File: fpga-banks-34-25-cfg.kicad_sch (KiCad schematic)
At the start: 49 parts, among them J13 PinHeader_1x3_P2.54mm_Drill1.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, Q12 2N7002_SOT-23-3, Q13 2N7002_SOT-23-3, Q14 2N7002_SOT-23-3, Q15 2N7002_SOT-23-3, Q16 2N7002_SOT-23-3, U14 XC7A100T-FGG484

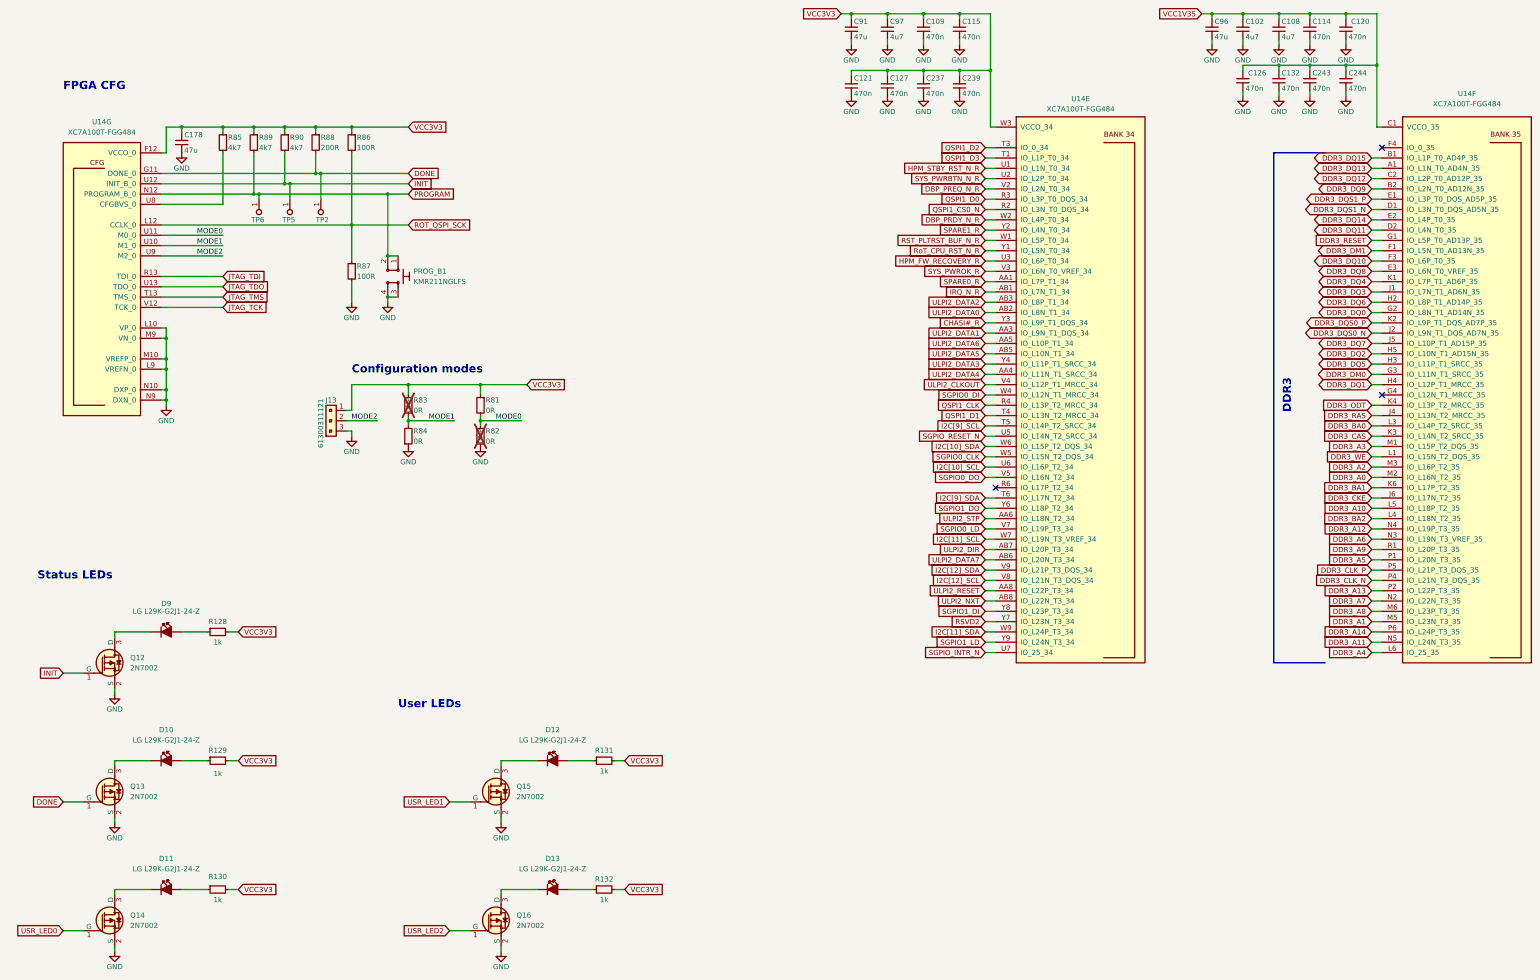
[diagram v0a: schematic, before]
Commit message: [#68236] Update symbols and footprints, clean ERC and DRC
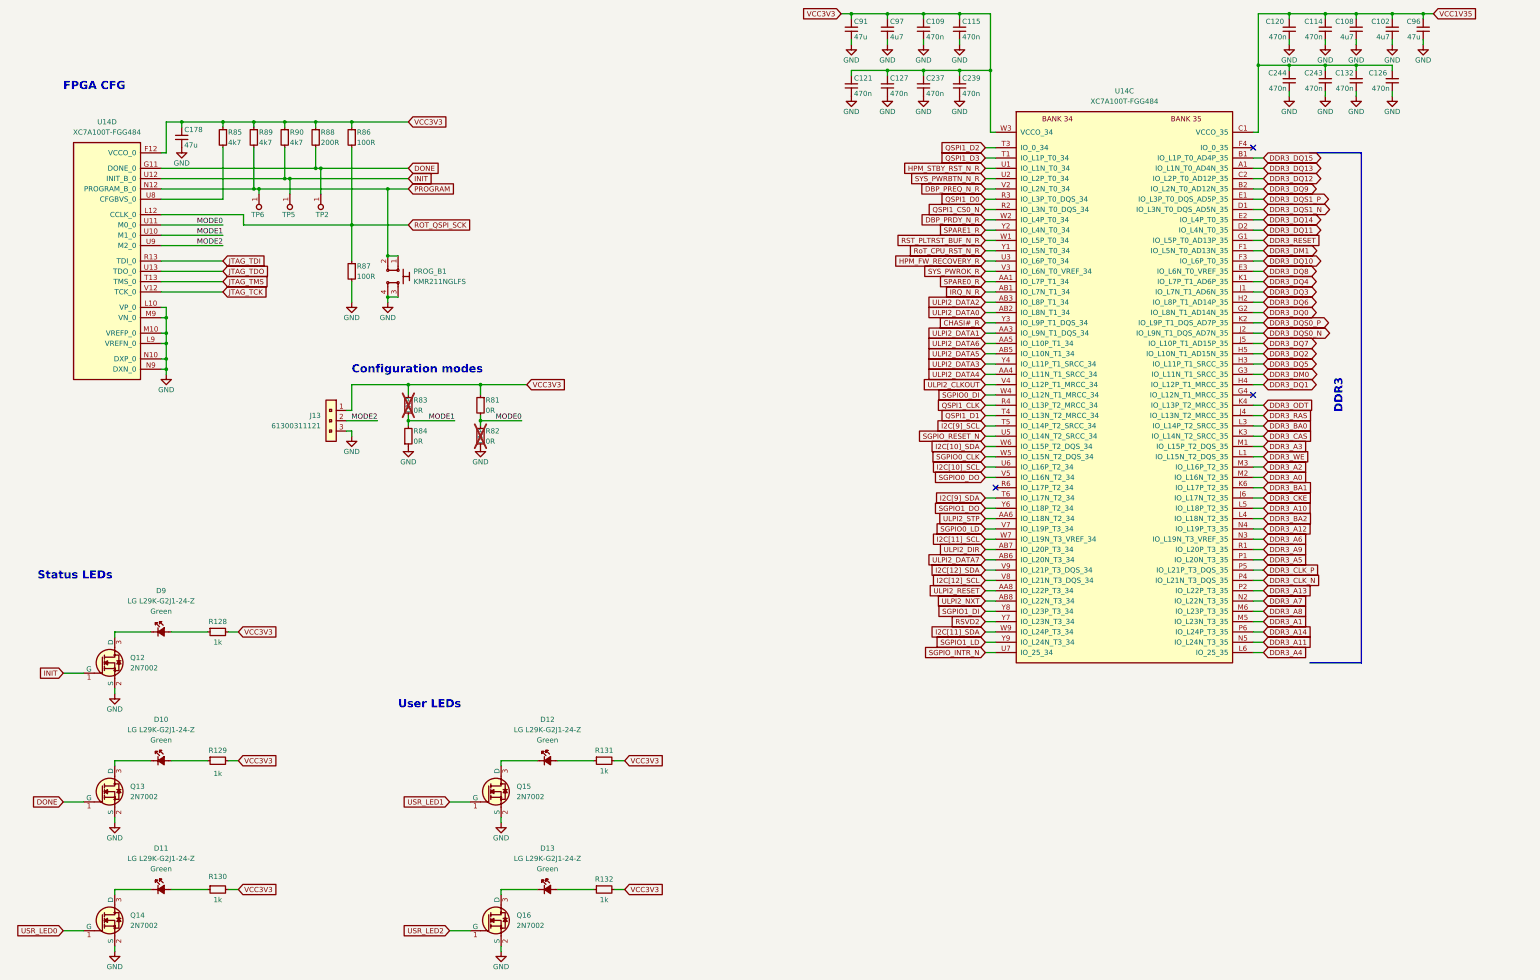
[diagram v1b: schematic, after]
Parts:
- removed unit 6 of U14
- removed unit 5 of U14
- added unit 3 of U14
- C178, C91, C96: Public (none) -> False
- D10, D11, D12, D13, D9: Color (none) -> Green
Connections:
- net CHASI#_R: now also U14.Y3 (IO_L9P_T1_DQS_34)
- net DBP_PRDY_N_R: now also U14.W2 (IO_L4P_T0_34)
- net DBP_PREQ_N_R: now also U14.V2 (IO_L2N_T0_34)
- net DDR3_A0: now also U14.M2 (IO_L16N_T2_35)
- net DDR3_A1: now also U14.M5 (IO_L23N_T3_35)
- net DDR3_A10: now also U14.L5 (IO_L18P_T2_35)
- net DDR3_A11: now also U14.N5 (IO_L24N_T3_35)
- net DDR3_A12: now also U14.N4 (IO_L19P_T3_35)
- net DDR3_A13: now also U14.P2 (IO_L22P_T3_35)
- net DDR3_A14: now also U14.P6 (IO_L24P_T3_35)
- net DDR3_A2: now also U14.M3 (IO_L16P_T2_35)
- net DDR3_A3: now also U14.M1 (IO_L15P_T2_DQS_35)
- net DDR3_A4: now also U14.L6 (IO_25_35)
- net DDR3_A5: now also U14.P1 (IO_L20N_T3_35)
- net DDR3_A6: now also U14.N3 (IO_L19N_T3_VREF_35)
- net DDR3_A7: now also U14.N2 (IO_L22N_T3_35)
- net DDR3_A8: now also U14.M6 (IO_L23P_T3_35)
- net DDR3_A9: now also U14.R1 (IO_L20P_T3_35)
- net DDR3_BA0: now also U14.L3 (IO_L14P_T2_SRCC_35)
- net DDR3_BA1: now also U14.K6 (IO_L17P_T2_35)
- net DDR3_BA2: now also U14.L4 (IO_L18N_T2_35)
- net DDR3_CAS: now also U14.K3 (IO_L14N_T2_SRCC_35)
- net DDR3_CKE: now also U14.J6 (IO_L17N_T2_35)
- net DDR3_CLK_N: now also U14.P4 (IO_L21N_T3_DQS_35)
- net DDR3_CLK_P: now also U14.P5 (IO_L21P_T3_DQS_35)
- net DDR3_DM0: now also U14.G3 (IO_L11N_T1_SRCC_35)
- net DDR3_DM1: now also U14.F1 (IO_L5N_T0_AD13N_35)
- net DDR3_DQ0: now also U14.G2 (IO_L8N_T1_AD14N_35)
- net DDR3_DQ1: now also U14.H4 (IO_L12P_T1_MRCC_35)
- net DDR3_DQ10: now also U14.F3 (IO_L6P_T0_35)
- net DDR3_DQ11: now also U14.D2 (IO_L4N_T0_35)
- net DDR3_DQ12: now also U14.C2 (IO_L2P_T0_AD12P_35)
- net DDR3_DQ13: now also U14.A1 (IO_L1N_T0_AD4N_35)
- net DDR3_DQ14: now also U14.E2 (IO_L4P_T0_35)
- net DDR3_DQ15: now also U14.B1 (IO_L1P_T0_AD4P_35)
- net DDR3_DQ2: now also U14.H5 (IO_L10N_T1_AD15N_35)
- net DDR3_DQ3: now also U14.J1 (IO_L7N_T1_AD6N_35)
- net DDR3_DQ4: now also U14.K1 (IO_L7P_T1_AD6P_35)
- net DDR3_DQ5: now also U14.H3 (IO_L11P_T1_SRCC_35)
- net DDR3_DQ6: now also U14.H2 (IO_L8P_T1_AD14P_35)
- net DDR3_DQ7: now also U14.J5 (IO_L10P_T1_AD15P_35)
- net DDR3_DQ8: now also U14.E3 (IO_L6N_T0_VREF_35)
- net DDR3_DQ9: now also U14.B2 (IO_L2N_T0_AD12N_35)
- net DDR3_DQS0_N: now also U14.J2 (IO_L9N_T1_DQS_AD7N_35)
- net DDR3_DQS0_P: now also U14.K2 (IO_L9P_T1_DQS_AD7P_35)
- net DDR3_DQS1_N: now also U14.D1 (IO_L3N_T0_DQS_AD5N_35)
- net DDR3_DQS1_P: now also U14.E1 (IO_L3P_T0_DQS_AD5P_35)
- net DDR3_ODT: now also U14.K4 (IO_L13P_T2_MRCC_35)
- net DDR3_RAS: now also U14.J4 (IO_L13N_T2_MRCC_35)
- net DDR3_RESET: now also U14.G1 (IO_L5P_T0_AD13P_35)
- net DDR3_WE: now also U14.L1 (IO_L15N_T2_DQS_35)
- net HPM_FW_RECOVERY_R: now also U14.U3 (IO_L6P_T0_34)
- net HPM_STBY_RST_N_R: now also U14.U1 (IO_L1N_T0_34)
- net I2C[10]_SCL: now also U14.U6 (IO_L16P_T2_34)
- net I2C[10]_SDA: now also U14.W6 (IO_L15P_T2_DQS_34)
- net I2C[11]_SCL: now also U14.W7 (IO_L19N_T3_VREF_34)
- net I2C[11]_SDA: now also U14.W9 (IO_L24P_T3_34)
- net I2C[12]_SCL: now also U14.V8 (IO_L21N_T3_DQS_34)
- net I2C[12]_SDA: now also U14.V9 (IO_L21P_T3_DQS_34)
- net I2C[9]_SCL: now also U14.T5 (IO_L14P_T2_SRCC_34)
- net I2C[9]_SDA: now also U14.T6 (IO_L17N_T2_34)
- net IRQ_N_R: now also U14.AB1 (IO_L7N_T1_34)
- net QSPI1_CLK: now also U14.R4 (IO_L13P_T2_MRCC_34)
- net QSPI1_CS0_N: now also U14.R2 (IO_L3N_T0_DQS_34)
- net QSPI1_D0: now also U14.R3 (IO_L3P_T0_DQS_34)
- net QSPI1_D1: now also U14.T4 (IO_L13N_T2_MRCC_34)
- net QSPI1_D2: now also U14.T3 (IO_0_34)
- net QSPI1_D3: now also U14.T1 (IO_L1P_T0_34)
- net RST_PLTRST_BUF_N_R: now also U14.W1 (IO_L5P_T0_34)
- net RSVD2: now also U14.Y7 (IO_L23N_T3_34)
- net RoT_CPU_RST_N_R: now also U14.Y1 (IO_L5N_T0_34)
- net SGPIO0_CLK: now also U14.W5 (IO_L15N_T2_DQS_34)
- net SGPIO0_DI: now also U14.W4 (IO_L12N_T1_MRCC_34)
- net SGPIO0_DO: now also U14.V5 (IO_L16N_T2_34)
- net SGPIO0_LD: now also U14.V7 (IO_L19P_T3_34)
- net SGPIO1_DI: now also U14.Y8 (IO_L23P_T3_34)
- net SGPIO1_DO: now also U14.Y6 (IO_L18P_T2_34)
- net SGPIO1_LD: now also U14.Y9 (IO_L24N_T3_34)
- net SGPIO_INTR_N: now also U14.U7 (IO_25_34)
- net SGPIO_RESET_N: now also U14.U5 (IO_L14N_T2_SRCC_34)
- net SPARE0_R: now also U14.AA1 (IO_L7P_T1_34)
- net SPARE1_R: now also U14.Y2 (IO_L4N_T0_34)
- net SYS_PWRBTN_N_R: now also U14.U2 (IO_L2P_T0_34)
- net SYS_PWROK_R: now also U14.V3 (IO_L6N_T0_VREF_34)
- net ULPI2_CLKOUT: now also U14.V4 (IO_L12P_T1_MRCC_34)
- net ULPI2_DATA0: now also U14.AB2 (IO_L8N_T1_34)
- net ULPI2_DATA1: now also U14.AA3 (IO_L9N_T1_DQS_34)
- net ULPI2_DATA2: now also U14.AB3 (IO_L8P_T1_34)
- net ULPI2_DATA3: now also U14.Y4 (IO_L11P_T1_SRCC_34)
- net ULPI2_DATA4: now also U14.AA4 (IO_L11N_T1_SRCC_34)
- net ULPI2_DATA5: now also U14.AB5 (IO_L10N_T1_34)
- net ULPI2_DATA6: now also U14.AA5 (IO_L10P_T1_34)
- net ULPI2_DATA7: now also U14.AB6 (IO_L20N_T3_34)
- net ULPI2_DIR: now also U14.AB7 (IO_L20P_T3_34)
- net ULPI2_NXT: now also U14.AB8 (IO_L22N_T3_34)
- net ULPI2_RESET: now also U14.AA8 (IO_L22P_T3_34)
- net ULPI2_STP: now also U14.AA6 (IO_L18N_T2_34)
- net VCC1V35: now also U14.C1 (VCCO_35), U14.F2 (VCCO_35), U14.H6 (VCCO_35), U14.J3 (VCCO_35), U14.M4 (VCCO_35), U14.N1 (VCCO_35)
- net VCC3V3: now also U14.AA7 (VCCO_34), U14.AB4 (VCCO_34), U14.R5 (VCCO_34), U14.T2 (VCCO_34), U14.V6 (VCCO_34), U14.W3 (VCCO_34)
- net at R129.1: now also D10.2 (A); no longer D10.1
- net at Q13.3 (D): now also D10.1 (C); no longer D10.2
- net at Q16.3 (D): now also D13.1 (C); no longer D13.2
- net at Q15.3 (D): now also D12.1 (C); no longer D12.2
- net at R131.1: now also D12.2 (A); no longer D12.1
- net at D9.1 (C): now also Q12.3 (D); no longer R128.1
- net at D11.1 (C): now also Q14.3 (D); no longer R130.1
- net at R132.1: now also D13.2 (A); no longer D13.1
- net at D11.2 (A): now also R130.1; no longer Q14.3 (D)
- net at D9.2 (A): now also R128.1; no longer Q12.3 (D)
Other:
- moved on the sheet: C178, R85, R86, R88, R89, R90, TP2, TP5, TP6

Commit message: [#82378] Project refresh 81589
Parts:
- R82, R83: DNP DNP -> (none)

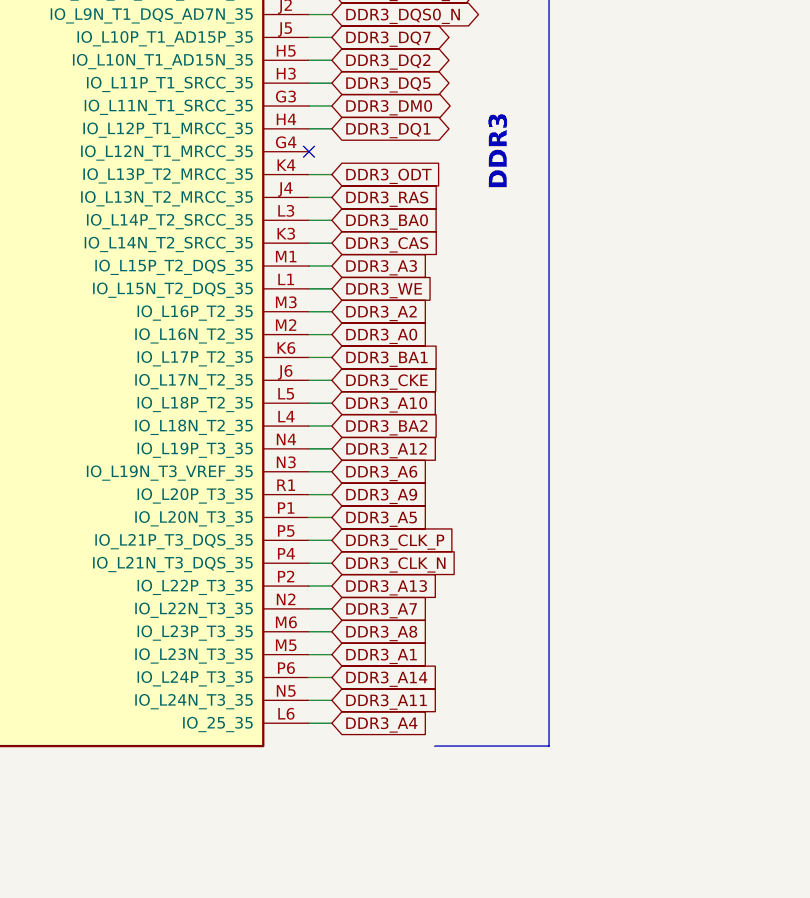
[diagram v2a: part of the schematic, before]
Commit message: started routing the ddr3 memory for defined stackup from Multi CB
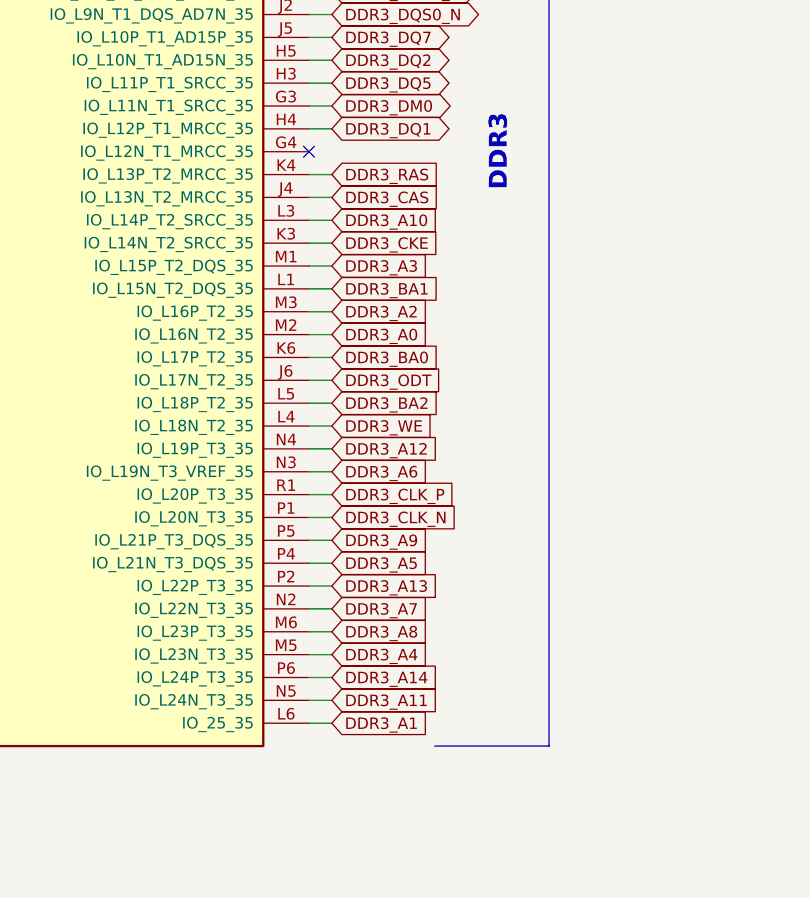
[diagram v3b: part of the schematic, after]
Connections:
- net DDR3_A1: now also U14.L6 (IO_25_35); no longer U14.M5 (IO_L23N_T3_35)
- net DDR3_A10: now also U14.L3 (IO_L14P_T2_SRCC_35); no longer U14.L5 (IO_L18P_T2_35)
- net DDR3_A4: now also U14.M5 (IO_L23N_T3_35); no longer U14.L6 (IO_25_35)
- net DDR3_A5: now also U14.P4 (IO_L21N_T3_DQS_35); no longer U14.P1 (IO_L20N_T3_35)
- net DDR3_A9: now also U14.P5 (IO_L21P_T3_DQS_35); no longer U14.R1 (IO_L20P_T3_35)
- net DDR3_BA0: now also U14.K6 (IO_L17P_T2_35); no longer U14.L3 (IO_L14P_T2_SRCC_35)
- net DDR3_BA1: now also U14.L1 (IO_L15N_T2_DQS_35); no longer U14.K6 (IO_L17P_T2_35)
- net DDR3_BA2: now also U14.L5 (IO_L18P_T2_35); no longer U14.L4 (IO_L18N_T2_35)
- net DDR3_CAS: now also U14.J4 (IO_L13N_T2_MRCC_35); no longer U14.K3 (IO_L14N_T2_SRCC_35)
- net DDR3_CKE: now also U14.K3 (IO_L14N_T2_SRCC_35); no longer U14.J6 (IO_L17N_T2_35)
- net DDR3_CLK_N: now also U14.P1 (IO_L20N_T3_35); no longer U14.P4 (IO_L21N_T3_DQS_35)
- net DDR3_CLK_P: now also U14.R1 (IO_L20P_T3_35); no longer U14.P5 (IO_L21P_T3_DQS_35)
- net DDR3_ODT: now also U14.J6 (IO_L17N_T2_35); no longer U14.K4 (IO_L13P_T2_MRCC_35)
- net DDR3_RAS: now also U14.K4 (IO_L13P_T2_MRCC_35); no longer U14.J4 (IO_L13N_T2_MRCC_35)
- net DDR3_WE: now also U14.L4 (IO_L18N_T2_35); no longer U14.L1 (IO_L15N_T2_DQS_35)
